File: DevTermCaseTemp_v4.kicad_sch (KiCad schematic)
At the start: 88 parts, among them J1 USB_A, J2 EXT_miniPCIe, J3 USB_A, J4 USB_B_Micro, J5 JBAT, J6 Conn_01x04, J7 DevTermSpeaker, J8 DevTermSpeaker, J9 Conn_02x22_Odd_Even, SW1 SW_DIP_x02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

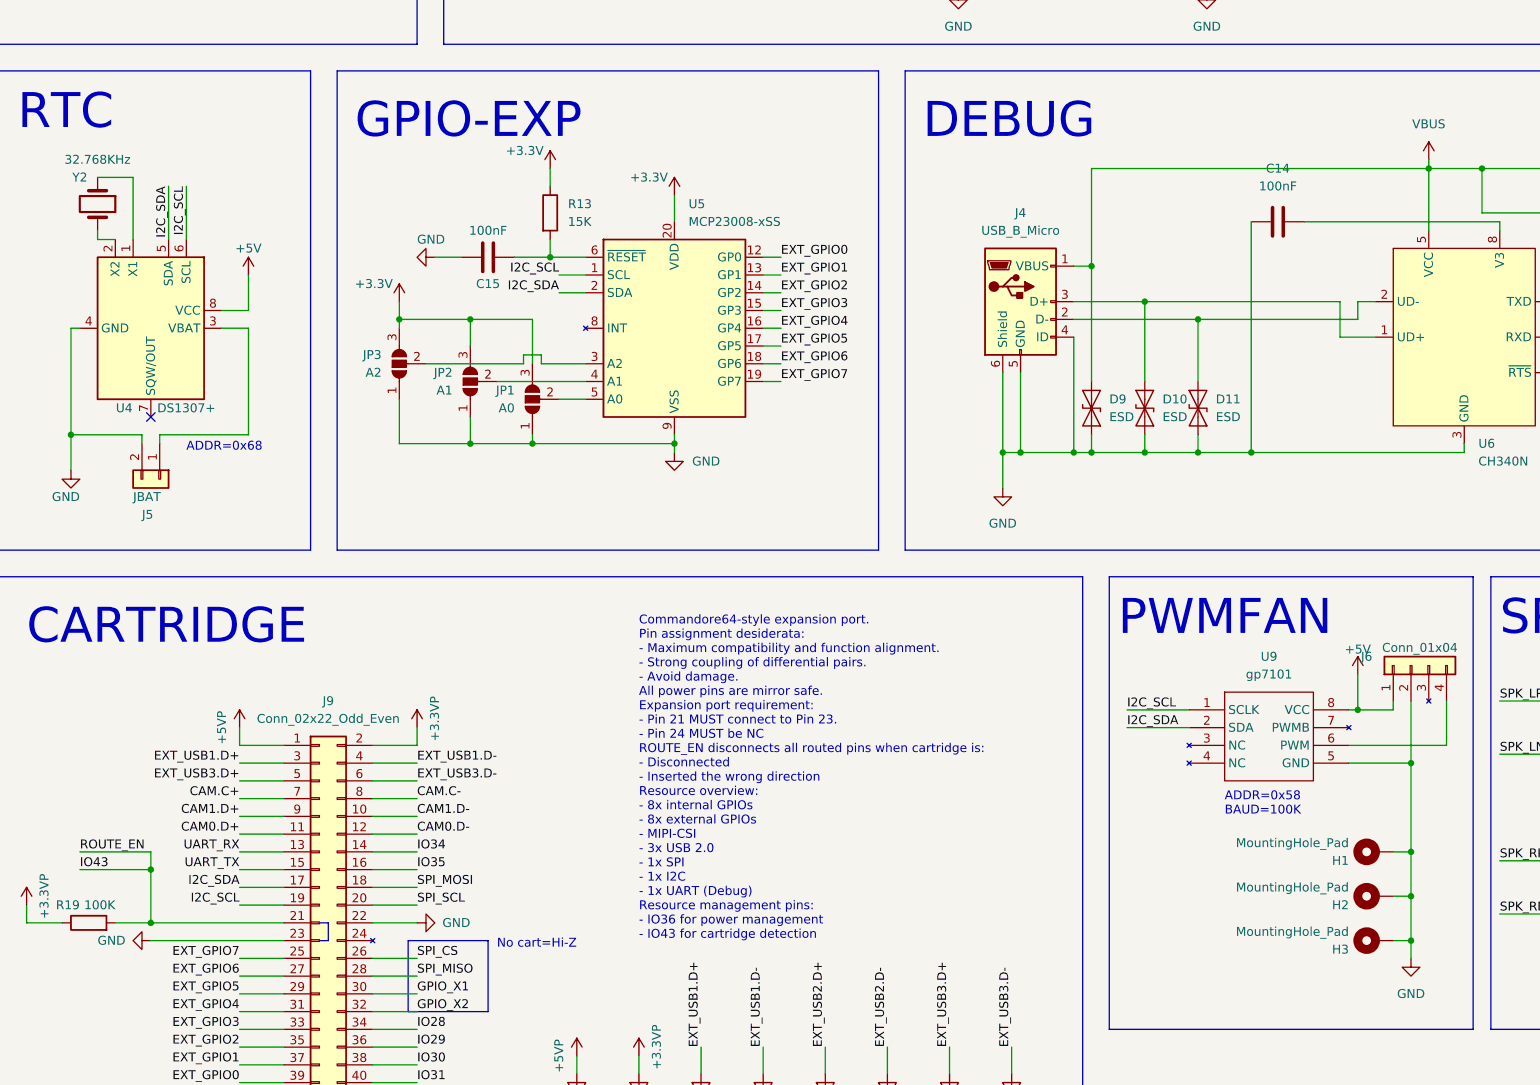
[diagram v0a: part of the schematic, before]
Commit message: turbo fan is now a component
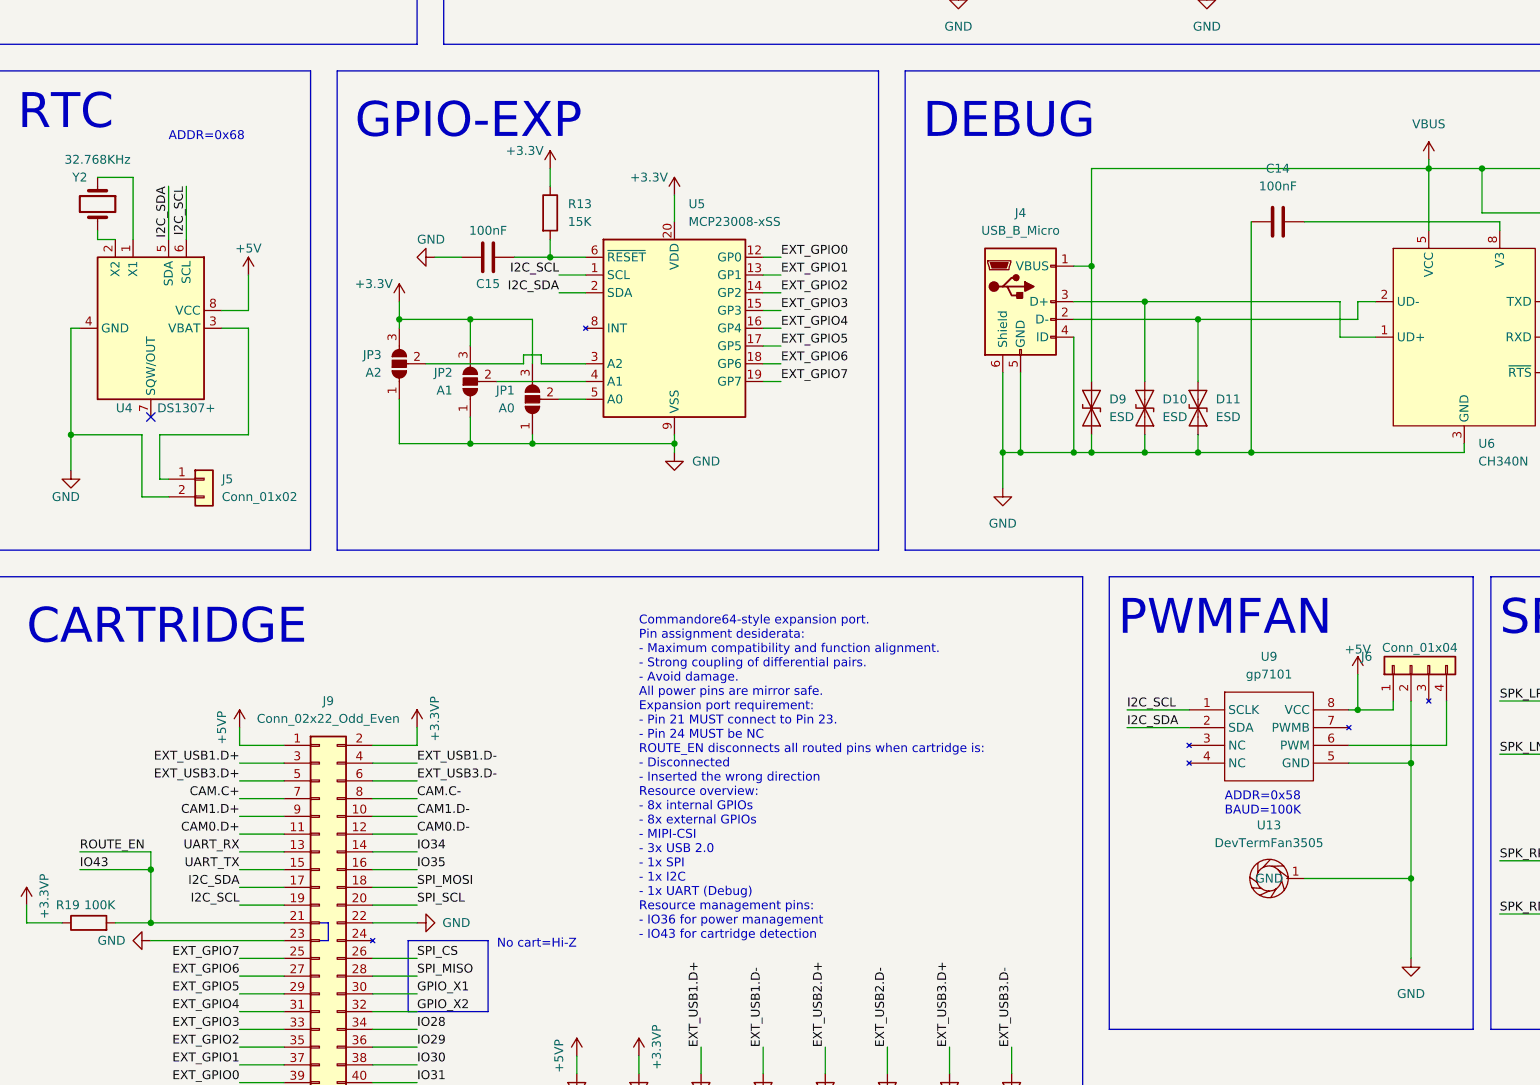
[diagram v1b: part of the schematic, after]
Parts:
- removed H1, H2, H3: MountingHole_Pad, MountingHole:MountingHole_2.7mm_M2.5_DIN965_Pad, symbol Mechanical:MountingHole_Pad
- added U13: DevTermFan3505, devterm-ext-outline:turbo_fan_3505, symbol devterm_symbols:DevTermFan3505
- J5: value JBAT -> Conn_01x02; footprint Connector_PinSocket_2.00mm:PinSocket_1x02_P2.00mm_Horizontal -> Connector_Molex:Molex_PicoBlade_53048-0210_1x02_P1.25mm_Horizontal
- J7, J8: symbol devterm_speaker:DevTermSpeaker -> devterm_symbols:DevTermSpeaker
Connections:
- net GND: now also U13.1 (GND)

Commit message: add ROUTE_EN pull down resistor
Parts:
- added R20: 10K, Resistor_SMD:R_0805_2012Metric, symbol Device:R
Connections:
- net GND: now also R20.1; no longer J9.23 (Pin_23)
- new net: J9.23 (Pin_23), R20.2
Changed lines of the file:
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@@
     (stroke (width 0) (type default) (color 0 0 0 0))
   )
+  (wire (pts (xy 156.21 247.65) (xy 156.21 250.19))
+    (stroke (width 0) (type default) (color 0 0 0 0))
+  )
   (wire (pts (xy 250.19 154.94) (xy 252.73 154.94))
     (stroke (width 0) (type default) (color 0 0 0 0))
@@
     (stroke (width 0) (type default) (color 0 0 0 0))
   )
+  (wire (pts (xy 156.21 237.49) (xy 181.61 237.49))
+    (stroke (width 0) (type default) (color 0 0 0 0))
+  )
   (wire (pts (xy 214.63 52.07) (xy 214.63 54.61))
     (stroke (width 0) (type default) (color 0 0 0 0))
@@
     (stroke (width 0) (type default) (color 0 0 0 0))
   )
+  (wire (pts (xy 156.21 240.03) (xy 156.21 237.49))
+    (stroke (width 0) (type default) (color 0 0 0 0))
+  )
   (wire (pts (xy 96.52 88.9) (xy 92.71 88.9))
     (stroke (width 0) (type default) (color 0 0 0 0))
@@
     (stroke (width 0) (type default) (color 0 0 0 0))
   )
-  (wire (pts (xy 162.56 237.49) (xy 181.61 237.49))
-    (stroke (width 0) (type default) (color 0 0 0 0))
-  )
   (polyline (pts (xy 15.24 281.94) (xy 137.16 281.94))
     (stroke (width 0) (type default) (color 0 0 0 0))
@@
     (pin "1")
   )
-  (symbol (lib_id "power:GND") (at 162.56 237.49 270) (unit 1)
+  (symbol (lib_id "power:GND") (at 156.21 250.19 0) (mirror y) (unit 1)
     (in_bom yes) (on_board yes)
-    (property "Reference" "#PWR053" (id 0) (at 156.21 237.49 0)
+    (property "Reference" "#PWR053" (id 0) (at 156.21 256.54 0)
       (effects (font (size 1.27 1.27)) hide)
     )
-    (property "Value" "GND" (id 1) (at 154.94 237.49 90)
+    (property "Value" "GND" (id 1) (at 156.21 257.81 90)
       (effects (font (size 1.27 1.27)) (justify left))
     )
-    (property "Footprint" "" (id 2) (at 162.56 237.49 0)
+    (property "Footprint" "" (id 2) (at 156.21 250.19 0)
       (effects (font (size 1.27 1.27)) hide)
     )
-    (property "Datasheet" "" (id 3) (at 162.56 237.49 0)
+    (property "Datasheet" "" (id 3) (at 156.21 250.19 0)
       (effects (font (size 1.27 1.27)) hide)
     )
@@
     (pin "1")
   )
+  (symbol (lib_id "Device:R") (at 156.21 243.84 180) (unit 1)
+    (in_bom yes) (on_board yes) (fields_autoplaced)
+    (property "Reference" "R20" (id 0) (at 158.75 242.5699 0)
+      (effects (font (size 1.27 1.27)) (justify right))
+    )
+    (property "Value" "10K" (id 1) (at 158.75 245.1099 0)
+      (effects (font (size 1.27 1.27)) (justify right))
+    )
+    (property "Footprint" "Resistor_SMD:R_0805_2012Metric" (id 2) (at 157.988 243.84 90)
+      (effects (font (size 1.27 1.27)) hide)
+    )
+    (property "Datasheet" "~" (id 3) (at 156.21 243.84 0)
+      (effects (font (size 1.27 1.27)) hide)
+    )
+    (pin "1")
+    (pin "2")
+  )
   (symbol (lib_id "power:GND") (at 285.75 266.7 0) (unit 1)
     (in_bom yes) (on_board yes)
@@
       (reference "R19") (unit 1) (value "100K") (footprint "Resistor_SMD:R_0805_2012Metric")
     )
+    (path "/da9004db-8e2b-4ffe-b1f9-7b95a792a525"
+      (reference "R20") (unit 1) (value "10K") (footprint "Resistor_SMD:R_0805_2012Metric")
+    )
     (path "/125fbcb6-842d-4f2b-ba67-5862a897bae9"
